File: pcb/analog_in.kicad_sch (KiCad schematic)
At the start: 21 parts, among them J7 Guitar Input, J8 Guitar Output, U5 TL072

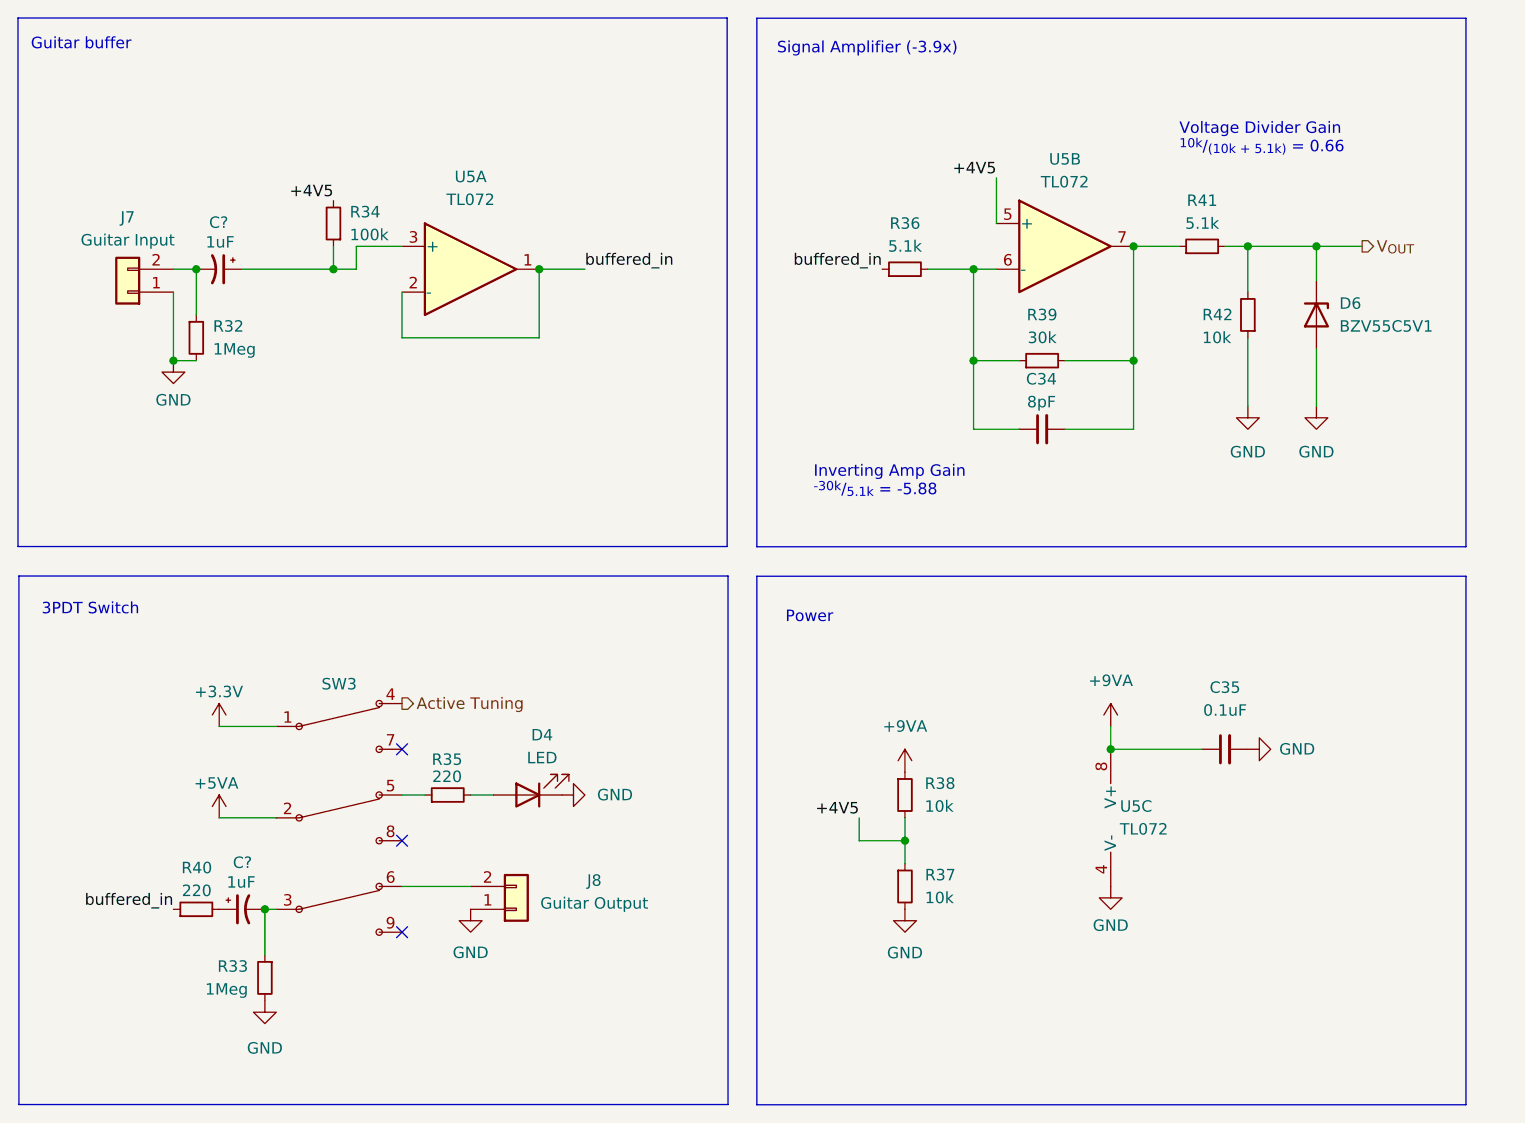
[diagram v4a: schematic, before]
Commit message: ERC fixes
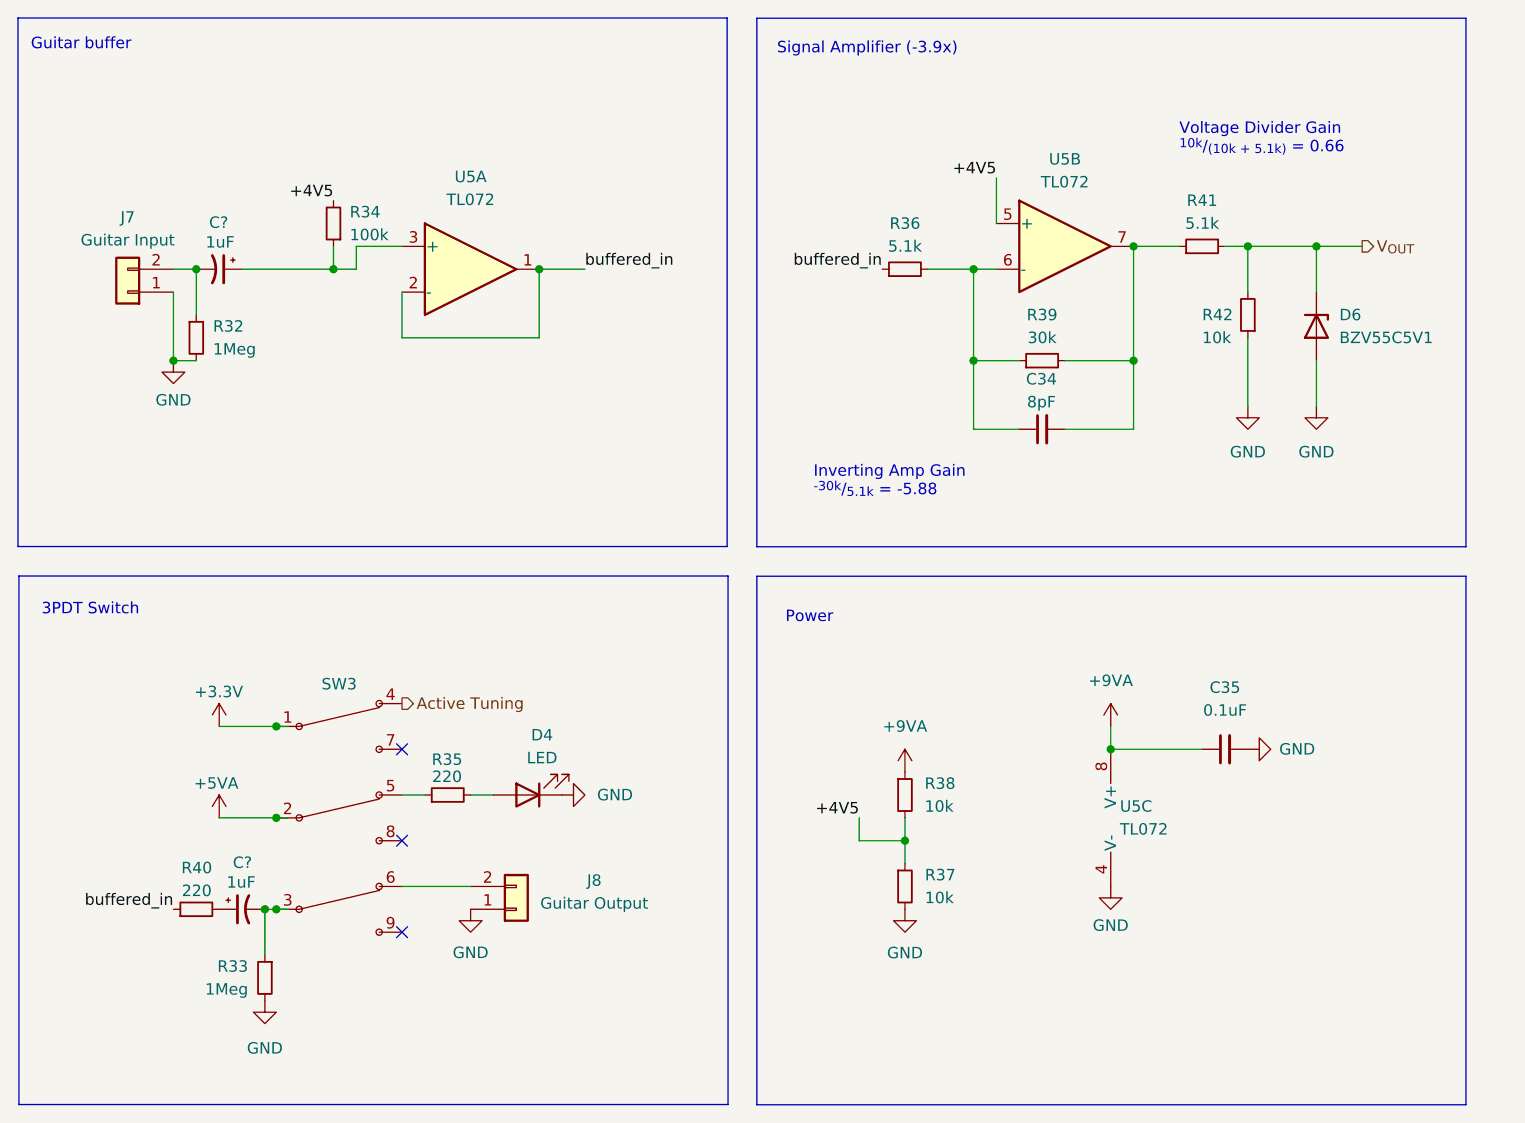
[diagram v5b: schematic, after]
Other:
- moved on the sheet: D6
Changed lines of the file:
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@@
   (junction (at 205.74 58.42) (diameter 0) (color 0 0 0 0)
   )
+  (junction (at 97.79 132.08) (diameter 0) (color 0 0 0 0)
+  )
   (junction (at 167.64 124.46) (diameter 0) (color 0 0 0 0)
   )
@@
   )
   (junction (at 175.26 60.96) (diameter 0) (color 0 0 0 0)
+  )
+  (junction (at 97.79 111.76) (diameter 0) (color 0 0 0 0)
+  )
+  (junction (at 97.79 121.92) (diameter 0) (color 0 0 0 0)
   )
   (no_connect (at 111.76 114.3))
@@
     (stroke (width 0) (type default))
   )
-  (wire (pts (xy 213.36 58.42) (xy 213.36 62.23))
+  (wire (pts (xy 213.36 58.42) (xy 213.36 63.5))
     (stroke (width 0) (type default))
   )
@@
     (stroke (width 0) (type default))
   )
+  (wire (pts (xy 97.79 132.08) (xy 99.06 132.08))
+    (stroke (width 0) (type default))
+  )
   (wire (pts (xy 175.26 71.12) (xy 175.26 60.96))
     (stroke (width 0) (type default))
@@
     (stroke (width 0) (type default))
   )
+  (wire (pts (xy 97.79 121.92) (xy 99.06 121.92))
+    (stroke (width 0) (type default))
+  )
   (wire (pts (xy 177.8 50.8) (xy 177.8 55.88))
     (stroke (width 0) (type default))
   )
+  (wire (pts (xy 97.79 111.76) (xy 99.06 111.76))
+    (stroke (width 0) (type default))
+  )
   (wire (pts (xy 180.34 71.12) (xy 175.26 71.12))
     (stroke (width 0) (type default))
@@
     (stroke (width 0) (type default))
   )
-  (wire (pts (xy 213.36 69.85) (xy 213.36 76.2))
+  (wire (pts (xy 213.36 71.12) (xy 213.36 76.2))
     (stroke (width 0) (type default))
   )
@@
     )
   )
-  (symbol (lib_id "Diode:BZV55C5V1") (at 213.36 66.04 270) (unit 1)
-    (in_bom yes) (on_board yes) (dnp no) (fields_autoplaced)
-    (property "Reference" "D6" (at 215.9 64.77 90)
-      (effects (font (size 1.27 1.27)) (justify left))
-    )
-    (property "Value" "BZV55C5V1" (at 215.9 67.31 90)
-      (effects (font (size 1.27 1.27)) (justify left))
-    )
-    (property "Footprint" "Diode_SMD:D_MiniMELF" (at 208.915 66.04 0)
-      (effects (font (size 1.27 1.27)) hide)
-    )
-    (property "Datasheet" "https://assets.nexperia.com/documents/data-sheet/BZV55_SER.pdf" (at 213.36 66.04 0)
-      (effects (font (size 1.27 1.27)) hide)
-    )
-    (property "LCSC" "C545327" (at 213.36 66.04 0)
-      (effects (font (size 1.27 1.27)) hide)
-    )
-    (property "MPN" "BZV55B5V1" (at 213.36 66.04 0)
-      (effects (font (size 1.27 1.27)) hide)
-    )
-    (property "Manufacturer" "LGE" (at 213.36 66.04 0)
-      (effects (font (size 1.27 1.27)) hide)
-    )
+  (symbol (lib_id "Diode:BZV55C5V1") (at 213.36 67.31 270) (unit 1)
+    (in_bom yes) (on_board yes) (dnp no) (fields_autoplaced)
+    (property "Reference" "D6" (at 215.9 66.04 90)
+      (effects (font (size 1.27 1.27)) (justify left))
+    )
+    (property "Value" "BZV55C5V1" (at 215.9 68.58 90)
+      (effects (font (size 1.27 1.27)) (justify left))
+    )
+    (property "Footprint" "Diode_SMD:D_MiniMELF" (at 208.915 67.31 0)
+      (effects (font (size 1.27 1.27)) hide)
+    )
+    (property "Datasheet" "https://assets.nexperia.com/documents/data-sheet/BZV55_SER.pdf" (at 213.36 67.31 0)
+      (effects (font (size 1.27 1.27)) hide)
+    )
+    (property "LCSC" "C545327" (at 213.36 67.31 0)
+      (effects (font (size 1.27 1.27)) hide)
+    )
+    (property "MPN" "BZV55B5V1" (at 213.36 67.31 0)
+      (effects (font (size 1.27 1.27)) hide)
+    )
+    (property "Manufacturer" "LGE" (at 213.36 67.31 0)
+      (effects (font (size 1.27 1.27)) hide)
+    )

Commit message: First revision of the pcb layout
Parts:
- C34: footprint Capacitor_SMD:C_0603_1608Metric -> Capacitor_SMD:C_0402_1005Metric; LCSC C346204 -> C1578; MPN CL10C080DB81PNC -> 0402CG8R0C500NT; Manufacturer Samsung Electro-Mechanics -> FH (Guangdong Fenghua Advanced Tech)
- C35: footprint Capacitor_SMD:C_1206_3216Metric -> Capacitor_SMD:C_0402_1005Metric; LCSC C577121 -> C1525; MPN CC1206JKNPO9BN104 -> CL05B104KO5NNNC; Manufacturer Yageo -> Samsung Electro-Mechanics
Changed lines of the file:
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@@
       (effects (font (size 1.27 1.27)))
     )
-    (property "Footprint" "Capacitor_SMD:C_0603_1608Metric" (at 182.88 78.74 0)
+    (property "Footprint" "Capacitor_SMD:C_0402_1005Metric" (at 182.88 78.74 0)
       (effects (font (size 1.27 1.27)) hide)
     )
@@
       (effects (font (size 1.27 1.27)) hide)
     )
-    (property "LCSC" "C346204" (at 182.88 78.74 0)
+    (property "LCSC" "C1578" (at 182.88 78.74 0)
       (effects (font (size 1.27 1.27)) hide)
     )
-    (property "MPN" "CL10C080DB81PNC" (at 182.88 78.74 0)
+    (property "MPN" "0402CG8R0C500NT" (at 182.88 78.74 0)
       (effects (font (size 1.27 1.27)) hide)
     )
-    (property "Manufacturer" "Samsung Electro-Mechanics" (at 182.88 78.74 0)
+    (property "Manufacturer" "FH (Guangdong Fenghua Advanced Tech)" (at 182.88 78.74 0)
       (effects (font (size 1.27 1.27)) hide)
     )
@@
       (effects (font (size 1.27 1.27)))
     )
-    (property "Footprint" "Capacitor_SMD:C_1206_3216Metric" (at 203.2 114.3 0)
+    (property "Footprint" "Capacitor_SMD:C_0402_1005Metric" (at 203.2 114.3 0)
       (effects (font (size 1.27 1.27)) hide)
     )
@@
       (effects (font (size 1.27 1.27)) hide)
     )
-    (property "LCSC" "C577121" (at 203.2 114.3 0)
+    (property "LCSC" "C1525" (at 203.2 114.3 0)
       (effects (font (size 1.27 1.27)) hide)
     )
-    (property "MPN" "CC1206JKNPO9BN104" (at 203.2 114.3 0)
+    (property "MPN" "CL05B104KO5NNNC" (at 203.2 114.3 0)
       (effects (font (size 1.27 1.27)) hide)
     )
-    (property "Manufacturer" "Yageo" (at 203.2 114.3 0)
+    (property "Manufacturer" "Samsung Electro-Mechanics" (at 203.2 114.3 0)
       (effects (font (size 1.27 1.27)) hide)
     )
